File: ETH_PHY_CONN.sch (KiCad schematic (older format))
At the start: 46 parts, among them J2 RJMG2012211A0FR, U7 DP83869HMRGZT, Y1 XRCGE25M000FBA1AR0

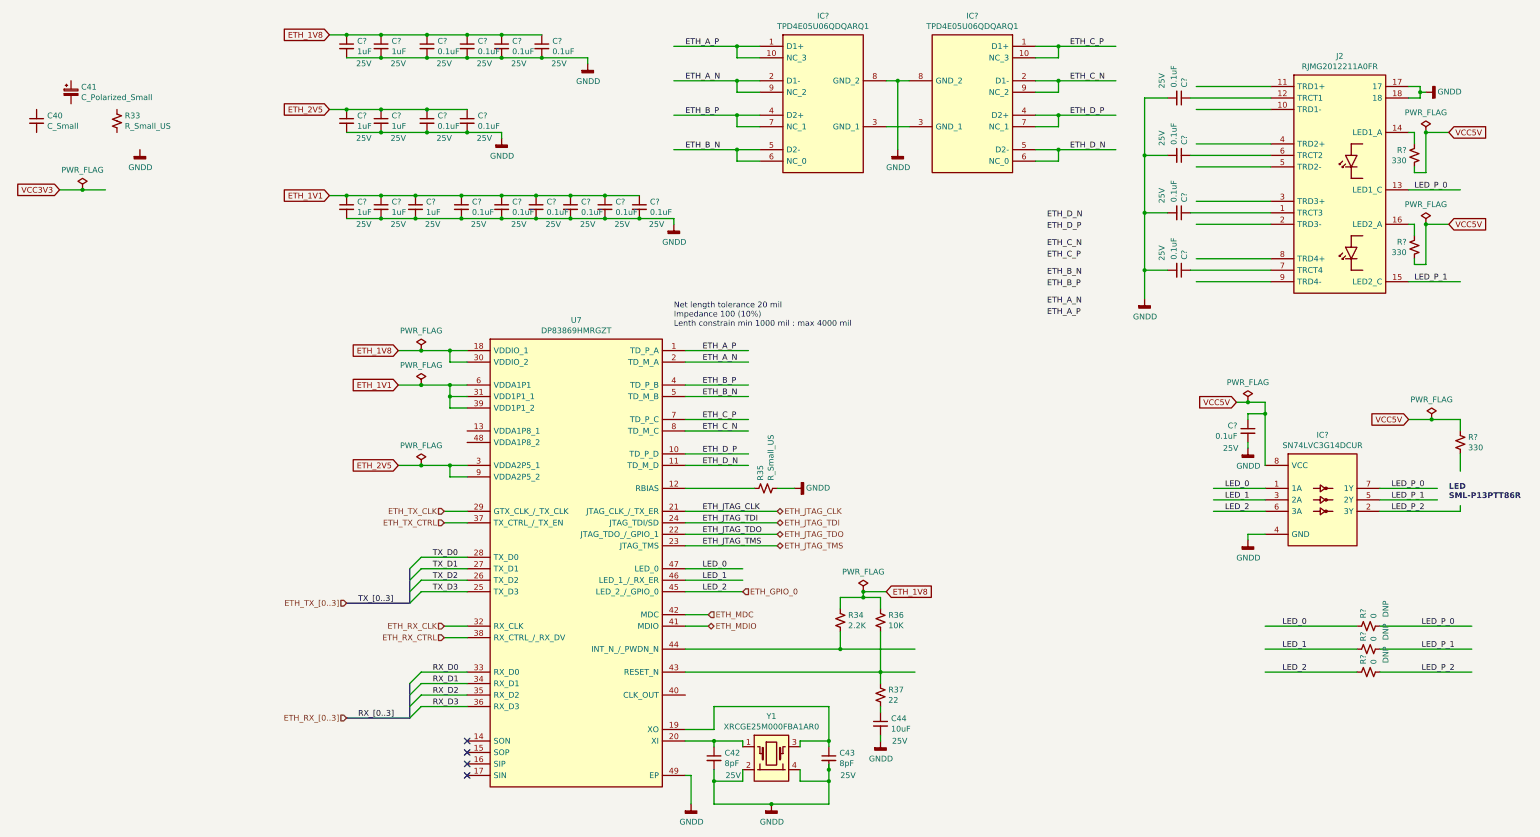
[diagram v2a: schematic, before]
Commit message: Drawn Eth power schematics and Eth PHY (continue)
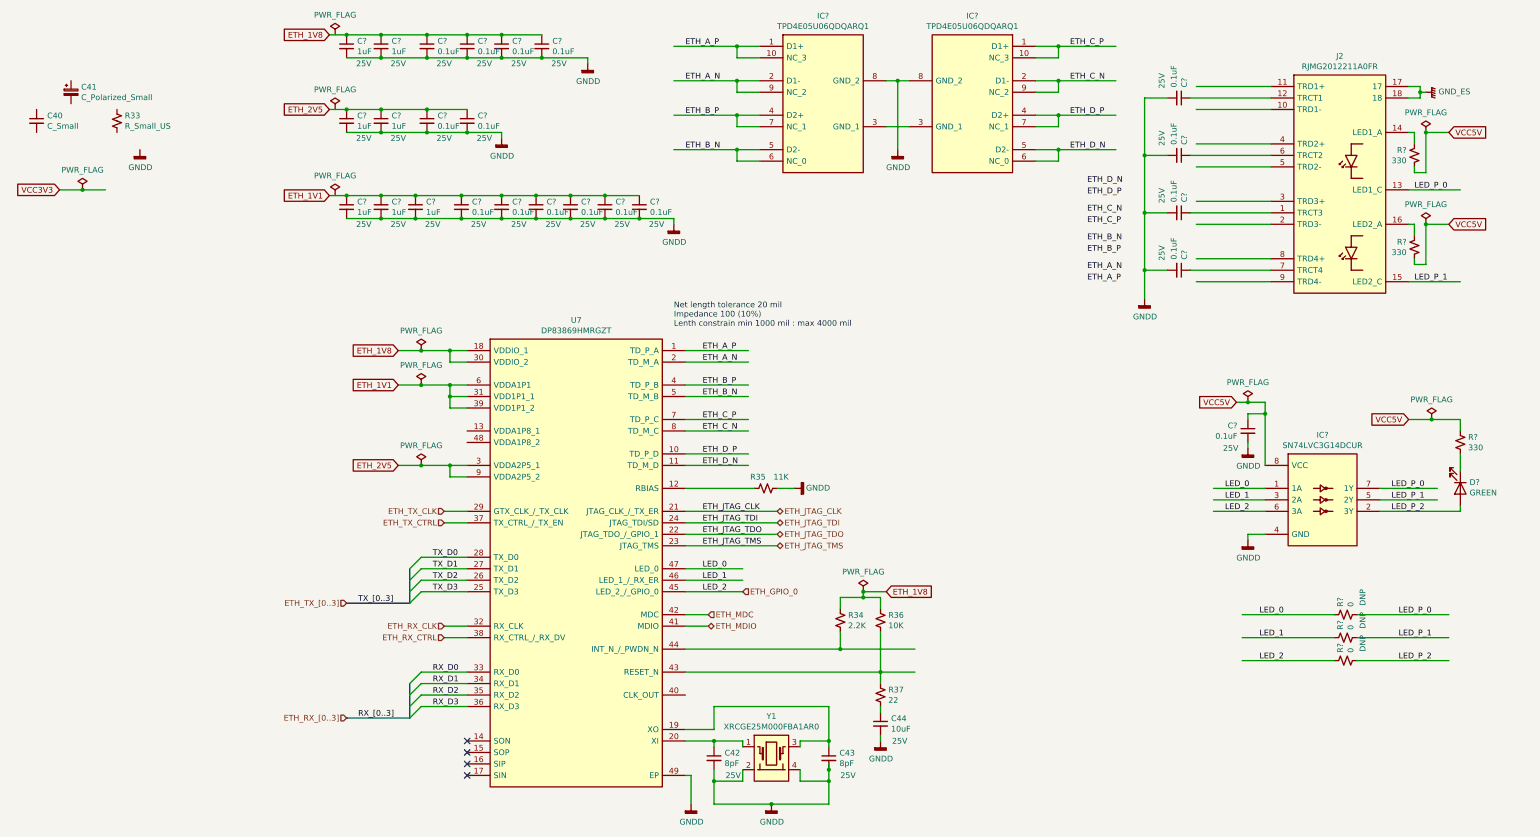
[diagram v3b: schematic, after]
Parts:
- added D?: GREEN, GM_LEDs:LEDC1006X25N, symbol Device:LED
- R35: value R_Small_US -> 11K
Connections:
- net labels added: GND_ES
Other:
- note removed: "LED\nSML-P13PTT86R"
- moved on the sheet: R?
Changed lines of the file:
@@
 AR Path="/601E7C92/6026D99A" Ref="R?"  Part="1"
 AR Path="/601E7C92/60257FE5/6026D99A" Ref="R35"  Part="1"
-F 0 "R35" H 4918 4746 50  0000 L CNN
-F 1 "R_Small_US" H 4918 4655 50  0000 L CNN
+F 0 "R35" V 4950 4700 50  0000 L CNN
+F 1 "11K" V 4950 4500 50  0000 L CNN
 F 2 "Resistor_SMD:R_0603_1608Metric_Pad0.98x0.95mm_HandSolder" H 4850 4700 50  0001 C CNN
 F 3 "~" H 4850 4700 50  0001 C CNN
@@
 $EndComp
 Wire Wire Line
-	9200 5900 10000 5900
-Wire Wire Line
-	9200 6100 10000 6100
-Wire Wire Line
-	9200 6300 10000 6300
-Text Label 9350 5900 0    50   ~ 0
+	9000 5800 9800 5800
+Wire Wire Line
+	9000 6000 9800 6000
+Wire Wire Line
+	9000 6200 9800 6200
+Text Label 9150 5800 0    50   ~ 0
 LED_0
-Text Label 9350 6100 0    50   ~ 0
+Text Label 9150 6000 0    50   ~ 0
 LED_1
-Text Label 9350 6300 0    50   ~ 0
+Text Label 9150 6200 0    50   ~ 0
 LED_2
 Wire Wire Line
-	11000 5900 10200 5900
-Wire Wire Line
-	11000 6100 10200 6100
-Wire Wire Line
-	11000 6300 10200 6300
-Text Label 10850 5900 2    50   ~ 0
+	10800 5800 10000 5800
+Wire Wire Line
+	10800 6000 10000 6000
+Wire Wire Line
+	10800 6200 10000 6200
+Text Label 10650 5800 2    50   ~ 0
 LED_P_0
-Text Label 10850 6100 2    50   ~ 0
+Text Label 10650 6000 2    50   ~ 0
 LED_P_1
-Text Label 10850 6300 2    50   ~ 0
+Text Label 10650 6200 2    50   ~ 0
 LED_P_2
 $Comp
 L Device:R_Small_US R?
 U 1 1 602AD488
-P 10100 5900
+P 9900 5800
 AR Path="/601E7C5A/602AD488" Ref="R?"  Part="1"
 AR Path="/601E7CC8/602AD488" Ref="R?"  Part="1"
 AR Path="/601E7C92/602AD488" Ref="R?"  Part="1"
 AR Path="/601E7C92/60257FE5/602AD488" Ref="R?"  Part="1"
-F 0 "R?" H 10168 5946 50  0000 L CNN
-F 1 "0" H 10168 5855 50  0000 L CNN
-F 2 "Resistor_SMD:R_0603_1608Metric_Pad0.98x0.95mm_HandSolder" H 10100 5900 50  0001 C CNN
-F 3 "~" H 10100 5900 50  0001 C CNN
-F 4 "DNP" H 10250 5750 50  0000 C CNN "DNP"
-	1    10100 5900
+F 0 "R?" H 9968 5846 50  0000 L CNN
+F 1 "0" H 9968 5755 50  0000 L CNN
+F 2 "Resistor_SMD:R_0603_1608Metric_Pad0.98x0.95mm_HandSolder" H 9900 5800 50  0001 C CNN
+F 3 "~" H 9900 5800 50  0001 C CNN
+F 4 "DNP" H 10050 5650 50  0000 C CNN "DNP"
+	1    9900 5800
 	0    -1   -1   0
 $EndComp
@@
 L Device:R_Small_US R?
 U 1 1 602CAD74
-P 10100 6100
+P 9900 6000
 AR Path="/601E7C5A/602CAD74" Ref="R?"  Part="1"
 AR Path="/601E7CC8/602CAD74" Ref="R?"  Part="1"
 AR Path="/601E7C92/602CAD74" Ref="R?"  Part="1"
 AR Path="/601E7C92/60257FE5/602CAD74" Ref="R?"  Part="1"
-F 0 "R?" H 10168 6146 50  0000 L CNN
-F 1 "0" H 10168 6055 50  0000 L CNN
-F 2 "Resistor_SMD:R_0603_1608Metric_Pad0.98x0.95mm_HandSolder" H 10100 6100 50  0001 C CNN
-F 3 "~" H 10100 6100 50  0001 C CNN
-F 4 "DNP" H 10250 5950 50  0000 C CNN "DNP"
-	1    10100 6100
+F 0 "R?" H 9968 6046 50  0000 L CNN
+F 1 "0" H 9968 5955 50  0000 L CNN
+F 2 "Resistor_SMD:R_0603_1608Metric_Pad0.98x0.95mm_HandSolder" H 9900 6000 50  0001 C CNN
+F 3 "~" H 9900 6000 50  0001 C CNN
+F 4 "DNP" H 10050 5850 50  0000 C CNN "DNP"
+	1    9900 6000
 	0    -1   -1   0
 $EndComp
@@
 L Device:R_Small_US R?
 U 1 1 602D1234
-P 10100 6300
+P 9900 6200
 AR Path="/601E7C5A/602D1234" Ref="R?"  Part="1"
 AR Path="/601E7CC8/602D1234" Ref="R?"  Part="1"
 AR Path="/601E7C92/602D1234" Ref="R?"  Part="1"
 AR Path="/601E7C92/60257FE5/602D1234" Ref="R?"  Part="1"
-F 0 "R?" H 10168 6346 50  0000 L CNN
-F 1 "0" H 10168 6255 50  0000 L CNN
-F 2 "Resistor_SMD:R_0603_1608Metric_Pad0.98x0.95mm_HandSolder" H 10100 6300 50  0001 C CNN
-F 3 "~" H 10100 6300 50  0001 C CNN
-F 4 "DNP" H 10250 6150 50  0000 C CNN "DNP"
-	1    10100 6300
+F 0 "R?" H 9968 6246 50  0000 L CNN
+F 1 "0" H 9968 6155 50  0000 L CNN
+F 2 "Resistor_SMD:R_0603_1608Metric_Pad0.98x0.95mm_HandSolder" H 9900 6200 50  0001 C CNN
+F 3 "~" H 9900 6200 50  0001 C CNN
+F 4 "DNP" H 10050 6050 50  0000 C CNN "DNP"
+	1    9900 6200
 	0    -1   -1   0
 $EndComp
@@
 Wire Wire Line
 	10900 4400 10900 4550
-Text Notes 10800 4800 0    50   ~ 10
-LED\nSML-P13PTT86R
 $Comp
 L GM_Protection:TPD4E05U06QDQARQ1 IC?
@@
 	0    1    -1   0
 $EndComp
-$Comp
-L Device:C_Small C?
-U 1 1 60416C50
-P 8450 2800
-AR Path="/601E7C5A/60416C50" Ref="C?"  Part="1"
-AR Path="/601E7CC8/60416C50" Ref="C?"  Part="1"
-AR Path="/601E7C92/60416C50" Ref="C?"  Part="1"
-AR Path="/601E7C92/60257FE5/60416C50" Ref="C?"  Part="1"
-F 0 "C?" H 8542 2846 50  0000 L CNN
-F 1 "0.1uF" H 8542 2755 50  0000 L CNN
-F 2 "Capacitor_SMD:C_0603_1608Metric_Pad1.08x0.95mm_HandSolder" H 8450 2800 50  0001 C CNN
-F 3 "~" H 8450 2800 50  0001 C CNN
-F 4 "25V" H 8600 2650 50  0000 C CNN "Voltage"
-	1    8450 2800
-	0    1    -1   0
-$EndComp
 Wire Wire Line
 	9250 1300 8550 1300
@@
 Wire Wire Line
 	10450 2900 10900 2900
-Text Label 7300 3200 0    50   ~ 0
+Text Label 7650 2900 0    50   ~ 0
 ETH_A_P
-Text Label 7300 3100 0    50   ~ 0
+Text Label 7650 2800 0    50   ~ 0
 ETH_A_N
-Text Label 7300 2950 0    50   ~ 0
+Text Label 7650 2650 0    50   ~ 0
 ETH_B_P
-Text Label 7300 2850 0    50   ~ 0
+Text Label 7650 2550 0    50   ~ 0
 ETH_B_N
-Text Label 7300 2700 0    50   ~ 0
+Text Label 7650 2400 0    50   ~ 0
 ETH_C_P
-Text Label 7300 2600 0    50   ~ 0
+Text Label 7650 2300 0    50   ~ 0
 ETH_C_N
-Text Label 7300 2450 0    50   ~ 0
+Text Label 7650 2150 0    50   ~ 0
 ETH_D_P
-Text Label 7300 2350 0    50   ~ 0
+Text Label 7650 2050 0    50   ~ 0
 ETH_D_N
 Text GLabel 10800 1600 2    50   Input ~ 0
@@
 	10450 1300 10550 1300
 Wire Wire Line
-	10550 1300 10550 1250
-Wire Wire Line
 	10550 1200 10450 1200
-Wire Wire Line
-	10550 1250 10600 1250
-Connection ~ 10550 1250
-Wire Wire Line
-	10550 1250 10550 1200
-$Comp
-L power:GNDD #PWR?
-U 1 1 604C465C
-P 10600 1250
-AR Path="/601DF0A6/604C465C" Ref="#PWR?"  Part="1"
-AR Path="/601E7C5A/604C465C" Ref="#PWR?"  Part="1"
-AR Path="/601E7CC8/604C465C" Ref="#PWR?"  Part="1"
-AR Path="/601E7C92/604C465C" Ref="#PWR?"  Part="1"
-AR Path="/601E7C92/60257FE5/604C465C" Ref="#PWR?"  Part="1"
-F 0 "#PWR?" H 10600 1000 50  0001 C CNN
-F 1 "GNDD" V 10604 1149 50  0000 R CNN
-F 2 "" H 10600 1250 50  0001 C CNN
-F 3 "" H 10600 1250 50  0001 C CNN
-	1    10600 1250
-	0    -1   -1   0
-$EndComp
 Text GLabel 1050 750  0    50   Input ~ 0
 ETH_1V8
@@
 Text GLabel 5900 5600 2    50   Input ~ 0
 ETH_1V8
+$Comp
+L Device:LED D?
+U 1 1 602A865B
+P 10900 4700
+F 0 "D?" V 10847 4780 50  0000 L CNN
+F 1 "GREEN" V 10938 4780 50  0000 L CNN
+F 2 "GM_LEDs:LEDC1006X25N" H 10900 4700 50  0001 C CNN
+F 3 "https://d1d2qsbl8m0m72.cloudfront.net/en/products/databook/datasheet/opto/led/chip_mono/sml-p1-e.pdf" H 10900 4700 50  0001 C CNN
+F 4 "SML-P13PTT86R" V 10900 4700 50  0001 C CNN "MPN"
+	1    10900 4700
+	0    1    1    0
+$EndComp
+$Comp
+L power:PWR_FLAG #FLG?
+U 1 1 603371CF
+P 1100 750
+AR Path="/601E7C5A/603371CF" Ref="#FLG?"  Part="1"
+AR Path="/601E7CC8/603371CF" Ref="#FLG?"  Part="1"
+AR Path="/601E7C92/603371CF" Ref="#FLG?"  Part="1"
+AR Path="/601E7C92/60257FE5/603371CF" Ref="#FLG?"  Part="1"
+F 0 "#FLG?" H 1100 825 50  0001 C CNN
+F 1 "PWR_FLAG" H 1100 923 50  0000 C CNN
+F 2 "" H 1100 750 50  0001 C CNN
+F 3 "~" H 1100 750 50  0001 C CNN
+	1    1100 750
+	1    0    0    -1
+$EndComp
+$Comp
+L power:PWR_FLAG #FLG?
+U 1 1 6034986B
+P 1100 1400
+AR Path="/601E7C5A/6034986B" Ref="#FLG?"  Part="1"
+AR Path="/601E7CC8/6034986B" Ref="#FLG?"  Part="1"
+AR Path="/601E7C92/6034986B" Ref="#FLG?"  Part="1"
+AR Path="/601E7C92/60257FE5/6034986B" Ref="#FLG?"  Part="1"
+F 0 "#FLG?" H 1100 1475 50  0001 C CNN
+F 1 "PWR_FLAG" H 1100 1573 50  0000 C CNN
+F 2 "" H 1100 1400 50  0001 C CNN
+F 3 "~" H 1100 1400 50  0001 C CNN
+	1    1100 1400
+	1    0    0    -1
+$EndComp
+$Comp
+L power:PWR_FLAG #FLG?
+U 1 1 6035C012
+P 1100 2150
+AR Path="/601E7C5A/6035C012" Ref="#FLG?"  Part="1"
+AR Path="/601E7CC8/6035C012" Ref="#FLG?"  Part="1"
+AR Path="/601E7C92/6035C012" Ref="#FLG?"  Part="1"
+AR Path="/601E7C92/60257FE5/6035C012" Ref="#FLG?"  Part="1"
+F 0 "#FLG?" H 1100 2225 50  0001 C CNN
+F 1 "PWR_FLAG" H 1100 2323 50  0000 C CNN
+F 2 "" H 1100 2150 50  0001 C CNN
+F 3 "~" H 1100 2150 50  0001 C CNN
+	1    1100 2150
+	1    0    0    -1
+$EndComp
+$Comp
+L Device:C_Small C?
+U 1 1 60416C50
+P 8450 2800
+AR Path="/601E7C5A/60416C50" Ref="C?"  Part="1"
+AR Path="/601E7CC8/60416C50" Ref="C?"  Part="1"
+AR Path="/601E7C92/60416C50" Ref="C?"  Part="1"
+AR Path="/601E7C92/60257FE5/60416C50" Ref="C?"  Part="1"
+F 0 "C?" H 8542 2846 50  0000 L CNN
+F 1 "0.1uF" H 8542 2755 50  0000 L CNN
+F 2 "Capacitor_SMD:C_0603_1608Metric_Pad1.08x0.95mm_HandSolder" H 8450 2800 50  0001 C CNN
+F 3 "~" H 8450 2800 50  0001 C CNN
+F 4 "25V" H 8600 2650 50  0000 C CNN "Voltage"
+	1    8450 2800
+	0    1    -1   0
+$EndComp
+Connection ~ 10550 1250
+Wire Wire Line
+	10550 1250 10550 1200
+Wire Wire Line
+	10550 1300 10550 1250
+Wire Wire Line
+	10550 1250 10600 1250
+$Comp
+L GM_Power:GND_ES #PWR?
+U 1 1 606C09C9
+P 10600 1250
+F 0 "#PWR?" H 10600 1050 50  0001 C CNN
+F 1 "GND_ES" V 10605 1141 50  0000 R CNN
+F 2 "" H 10600 1200 50  0001 C CNN
+F 3 "" H 10600 1200 50  0001 C CNN
+	1    10600 1250
+	0    -1   -1   0
+$EndComp
 Wire Bus Line
 	1750 5400 1750 5700

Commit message: Drawn Ethernet PHY schematics
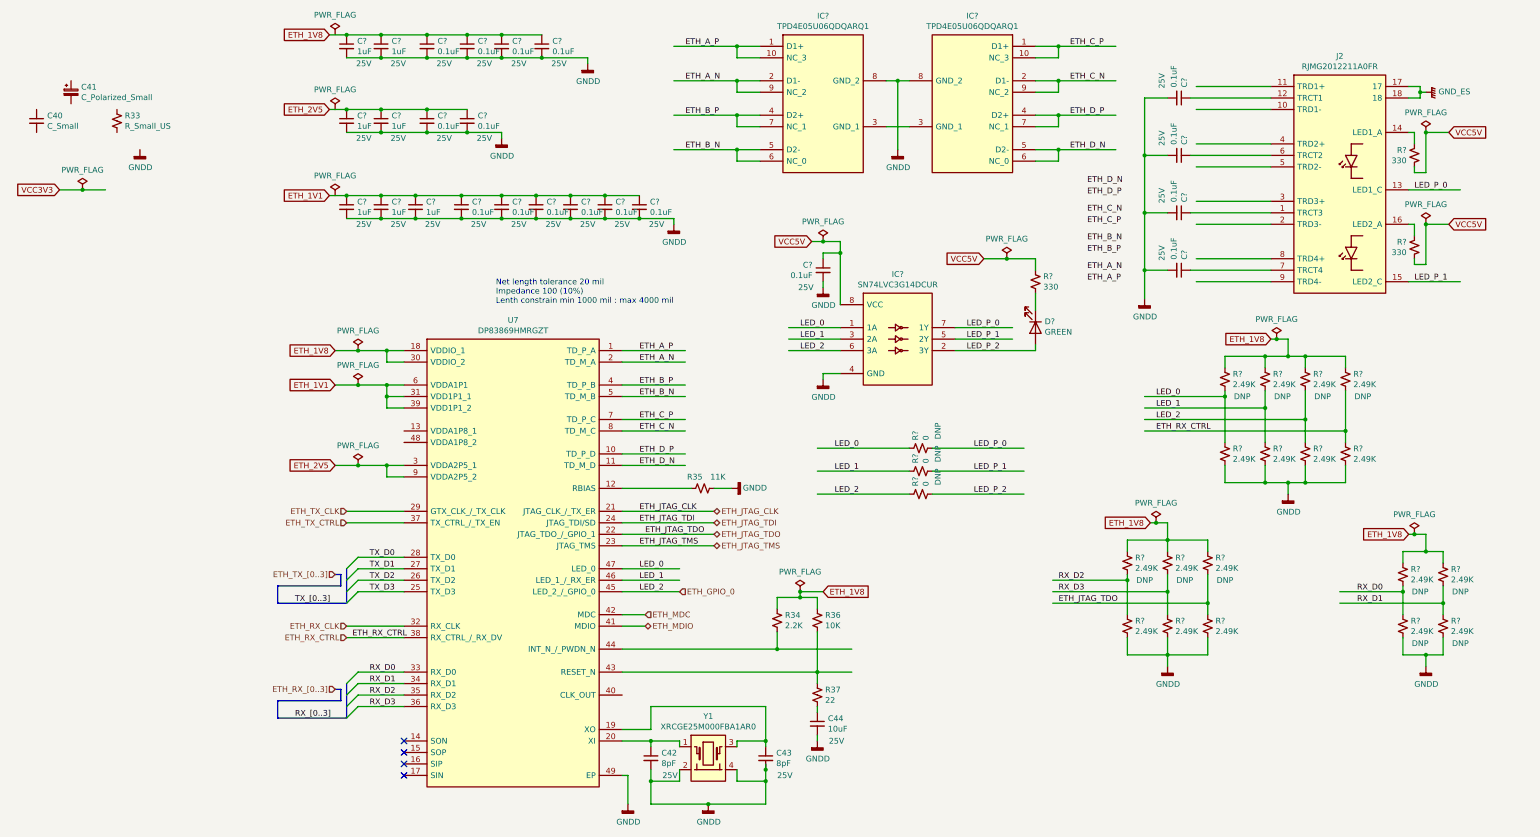
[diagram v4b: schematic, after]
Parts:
- added R? (x18): 2.49K, Resistor_SMD:R_0603_1608Metric_Pad0.98x0.95mm_HandSolder, symbol Device:R_Small_US
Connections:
- wire segments 231 -> 304
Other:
- moved on the sheet: C42, C43, C44, C?, D?, IC?, R34, R35, R36, R37, R?, U7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
